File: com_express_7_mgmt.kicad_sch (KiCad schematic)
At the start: 79 parts, among them J11 Plug_Bus_CE7_EPT_401-51501-51, J14 PinHeader_1x3_P2.54mm_Drill1.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, J15 PinHeader_1x3_P2.54mm_Drill1.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, Q3 BSS138-7-F, Q4 BSS138-7-F, SW1 SW_1-1825027-1_THT, SW2 SW_1-1825027-1_THT, U24 M24C64-F_DFN8, U25 TPS3840PL30DBVR, U26 74AUP2G132, U27 MAX16150A_SOT, U28 74AUP2G132, U29 W25Q32FV_SOIC-8, U32 74AUP2G132

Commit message: Fix ERC
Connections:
- net ~{SUS_S3} is gone; now on an unnamed net: J11.A15 (~{SUS_S3})
- net ~{SUS_S5}: now also J11.A24 (~{SUS_S5})
- net at TP36.1: no longer J11.A24 (~{SUS_S5})
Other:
- moved on the sheet: R138, TP36
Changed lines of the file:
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@@
   (junction (at 259.08 205.74) (diameter 0) (color 0 0 0 0)
   )
+  (junction (at 91.44 68.58) (diameter 0) (color 0 0 0 0)
+  )
   (junction (at 254 121.92) (diameter 0) (color 0 0 0 0)
   )
@@
   (junction (at 342.9 62.23) (diameter 0) (color 0 0 0 0)
   )
+  (junction (at 382.27 193.04) (diameter 0) (color 0 0 0 0)
+  )
   (junction (at 78.74 53.34) (diameter 0) (color 0 0 0 0)
   )
@@
     (stroke (width 0) (type default))
   )
-  (wire (pts (xy 76.2 167.64) (xy 93.98 167.64))
+  (wire (pts (xy 104.14 38.1) (xy 104.14 41.91))
     (stroke (width 0) (type default))
   )
-  (wire (pts (xy 104.14 38.1) (xy 104.14 41.91))
+  (bus (pts (xy 105.41 266.7) (xy 95.25 266.7))
     (stroke (width 0) (type default))
   )
@@
     (stroke (width 0) (type default))
   )
-  (wire (pts (xy 334.645 231.14) (xy 349.885 231.14))
+  (wire (pts (xy 335.28 231.14) (xy 350.52 231.14))
     (stroke (width 0) (type default))
   )
@@
     (stroke (width 0) (type default))
   )
-  (bus (pts (xy 95.25 266.7) (xy 96.52 266.7))
-    (stroke (width 0) (type default))
-  )
   (wire (pts (xy 245.11 223.52) (xy 250.19 223.52))
     (stroke (width 0) (type default))
@@
     (stroke (width 0) (type default))
   )
+  (wire (pts (xy 95.25 172.72) (xy 76.2 172.72))
+    (stroke (width 0) (type default))
+  )
   (wire (pts (xy 119.38 147.32) (xy 121.92 147.32))
     (stroke (width 0) (type default))
@@
     (stroke (width 0) (type default))
   )
-  (wire (pts (xy 354.965 231.14) (xy 360.68 231.14))
+  (wire (pts (xy 355.6 231.14) (xy 360.68 231.14))
     (stroke (width 0) (type default))
   )
@@
     (effects (font (size 1.27 1.27)) (justify right bottom))
   )
+  (label "I2C{I2C}" (at 105.41 266.7 180) (fields_autoplaced)
+    (effects (font (size 1.27 1.27)) (justify right bottom))
+  )
   (label "~{RESBTN}" (at 332.74 57.15 0) (fields_autoplaced)
     (effects (font (size 1.27 1.27)) (justify left bottom))
   )
+  (label "~{SUS_S5}" (at 95.25 172.72 180) (fields_autoplaced)
+    (effects (font (size 1.27 1.27)) (justify right bottom))
+  )
   (label "~{TYPE1}" (at 201.93 137.16 0) (fields_autoplaced)
     (effects (font (size 1.27 1.27)) (justify left bottom))
@@
     (effects (font (size 1.27 1.27)) (justify right bottom))
   )
-  (label "~{SUS_S3}" (at 93.98 167.64 180) (fields_autoplaced)
-    (effects (font (size 1.27 1.27)) (justify right bottom))
-  )
   (label "~{TYPE2}" (at 83.82 218.44 180) (fields_autoplaced)
     (effects (font (size 1.27 1.27)) (justify right bottom))
@@
     (effects (font (size 1.27 1.27)) (justify left bottom))
   )
-  (label "~{BIOS_DIS0}" (at 334.645 231.14 0) (fields_autoplaced)
+  (label "~{BIOS_DIS0}" (at 335.28 231.14 0) (fields_autoplaced)
     (effects (font (size 1.27 1.27)) (justify left bottom))
   )
@@
     (effects (font (size 1.27 1.27)) (justify left))
   )
-  (hierarchical_label "I2C{I2C}" (shape output) (at 96.52 266.7 0) (fields_autoplaced)
-    (effects (font (size 1.27 1.27)) (justify left))
-  )
   (hierarchical_label "SMBus{I2C}" (shape output) (at 99.06 151.13 0) (fields_autoplaced)
     (effects (font (size 1.27 1.27)) (justify left))
@@
     )
   )
-  (symbol (lib_id "antmicroResistors0402:R_1k_0402") (at 349.885 231.14 0) (unit 1)
+  (symbol (lib_id "antmicroResistors0402:R_1k_0402") (at 350.52 231.14 0) (unit 1)
     (in_bom yes) (on_board yes) (dnp no)
-    (property "Reference" "R138" (at 347.345 229.87 0)
+    (property "Reference" "R138" (at 347.98 229.87 0)
       (effects (font (size 1.27 1.27) (thickness 0.15)))
     )
-    (property "Value" "R_1k_0402" (at 370.205 243.84 0)
+    (property "Value" "R_1k_0402" (at 370.84 243.84 0)
       (effects (font (size 1.27 1.27) (thickness 0.15)) (justify left bottom) hide)
     )
-    (property "Footprint" "antmicro-footprints:R_0402_1005Metric" (at 370.205 246.38 0)
+    (property "Footprint" "antmicro-footprints:R_0402_1005Metric" (at 370.84 246.38 0)
       (effects (font (size 1.27 1.27) (thickness 0.15)) (justify left bottom) hide)
     )
-    (property "Datasheet" "https://www.bourns.com/docs/product-datasheets/cr.pdf" (at 370.205 248.92 0)
+    (property "Datasheet" "https://www.bourns.com/docs/product-datasheets/cr.pdf" (at 370.84 248.92 0)
       (effects (font (size 1.27 1.27) (thickness 0.15)) (justify left bottom) hide)
     )
-    (property "MPN" "CR0402-FX-1001GLF" (at 370.205 251.46 0)
+    (property "MPN" "CR0402-FX-1001GLF" (at 370.84 251.46 0)
       (effects (font (size 1.27 1.27) (thickness 0.15)) (justify left bottom) hide)
     )
-    (property "Manufacturer" "Bourns" (at 370.205 254 0)
+    (property "Manufacturer" "Bourns" (at 370.84 254 0)
       (effects (font (size 1.27 1.27) (thickness 0.15)) (justify left bottom) hide)
     )
-    (property "License" "Apache-2.0" (at 370.205 256.54 0)
+    (property "License" "Apache-2.0" (at 370.84 256.54 0)
       (effects (font (size 1.27 1.27) (thickness 0.15)) (justify left bottom) hide)
     )
-    (property "Author" "Antmicro" (at 370.205 259.08 0)
+    (property "Author" "Antmicro" (at 370.84 259.08 0)
       (effects (font (size 1.27 1.27) (thickness 0.15)) (justify left bottom) hide)
     )
-    (property "Val" "1k" (at 356.235 229.87 0)
+    (property "Val" "1k" (at 356.87 229.87 0)
       (effects (font (size 1.27 1.27) (thickness 0.15)))
     )
-    (property "Tolerance" "1%" (at 370.205 241.3 0)
+    (property "Tolerance" "1%" (at 370.84 241.3 0)
       (effects (font (size 1.27 1.27)) (justify left bottom) hide)
     )
@@
     )
   )
+  (symbol (lib_id "antmicropower:PWR_FLAG") (at 382.27 193.04 0) (unit 1)
+    (in_bom yes) (on_board yes) (dnp no) (fields_autoplaced)
+    (property "Reference" "#FLG016" (at 382.27 191.135 0)
+      (effects (font (size 1.27 1.27)) hide)
+    )
+    (property "Value" "PWR_FLAG" (at 382.27 187.96 0)
+      (effects (font (size 1.27 1.27)) hide)
+    )
+    (property "Footprint" "" (at 382.27 193.04 0)
+      (effects (font (size 1.27 1.27)) hide)
+    )
+    (property "Datasheet" "" (at 382.27 193.04 0)
+      (effects (font (size 1.27 1.27)) hide)
+    )
+    (pin "1")
+    (instances
+      (project "com-express-7-baseboard"
+        (path "/1b8c34da-dad5-4b0b-8c4b-45db766c4dfa/ec04a123-aeba-4efb-8d03-9c06245c1fcc"
+          (reference "#FLG016") (unit 1)
+        )
+      )
+    )
+  )
   (symbol (lib_id "antmicroTestPoints:TP_0.75mm_SMD") (at 76.2 124.46 0) (unit 1)
     (in_bom no) (on_board yes) (dnp no) (fields_autoplaced)
@@
     )
   )
+  (symbol (lib_id "antmicropower:PWR_FLAG") (at 91.44 68.58 270) (unit 1)
+    (in_bom yes) (on_board yes) (dnp no) (fields_autoplaced)
+    (property "Reference" "#FLG017" (at 93.345 68.58 0)
+      (effects (font (size 1.27 1.27)) hide)
+    )
+    (property "Value" "PWR_FLAG" (at 95.25 68.5799 90)
+      (effects (font (size 1.27 1.27)) (justify left) hide)
+    )
+    (property "Footprint" "" (at 91.44 68.58 0)
+      (effects (font (size 1.27 1.27)) hide)
+    )
+    (property "Datasheet" "" (at 91.44 68.58 0)
+      (effects (font (size 1.27 1.27)) hide)
+    )
+    (pin "1")
+    (instances
+      (project "com-express-7-baseboard"
+        (path "/1b8c34da-dad5-4b0b-8c4b-45db766c4dfa/ec04a123-aeba-4efb-8d03-9c06245c1fcc"
+          (reference "#FLG017") (unit 1)
+        )
+      )
+    )
+  )
   (symbol (lib_name "BAT54C_1") (lib_id "antmicroDiodesRectifiersSingle:BAT54C") (at 135.89 63.5 180) (unit 1)
     (in_bom yes) (on_board yes) (dnp no) (fields_autoplaced)
@@
     )
   )
-  (symbol (lib_id "antmicroTestPoints:TP_0.75mm_SMD") (at 76.2 172.72 0) (unit 1)
+  (symbol (lib_id "antmicroTestPoints:TP_0.75mm_SMD") (at 76.2 167.64 0) (unit 1)
     (in_bom no) (on_board yes) (dnp no) (fields_autoplaced)
-    (property "Reference" "TP36" (at 81.28 172.72 0)
+    (property "Reference" "TP36" (at 81.28 167.64 0)
       (effects (font (size 1.27 1.27) (thickness 0.15)) (justify left))
     )
-    (property "Value" "TP_0.75mm_SMD" (at 86.995 176.53 0)
+    (property "Value" "TP_0.75mm_SMD" (at 86.995 171.45 0)
       (effects (font (size 1.27 1.27) (thickness 0.15)) (justify left bottom) hide)
     )
-    (property "Footprint" "antmicro-footprints:TP_SMD_0.75mm" (at 86.995 179.07 0)
+    (property "Footprint" "antmicro-footprints:TP_SMD_0.75mm" (at 86.995 173.99 0)
       (effects (font (size 1.27 1.27) (thickness 0.15)) (justify left bottom) hide)
     )
-    (property "Datasheet" "" (at 93.98 185.42 0)
+    (property "Datasheet" "" (at 93.98 180.34 0)
       (effects (font (size 1.27 1.27) (thickness 0.15)) (justify left bottom) hide)
     )
-    (property "MPN" "" (at 86.995 184.15 0)
+    (property "MPN" "" (at 86.995 179.07 0)
       (effects (font (size 1.27 1.27) (thickness 0.15)) (justify left bottom) hide)
     )
-    (property "Manufacturer" "" (at 86.995 179.07 0)
+    (property "Manufacturer" "" (at 86.995 173.99 0)
       (effects (font (size 1.27 1.27) (thickness 0.15)) (justify left bottom) hide)
     )
-    (property "Author" "Antmicro" (at 86.995 181.61 0)
+    (property "Author" "Antmicro" (at 86.995 176.53 0)
       (effects (font (size 1.27 1.27) (thickness 0.15)) (justify left bottom) hide)
     )
-    (property "License" "Apache-2.0" (at 86.995 184.15 0)
+    (property "License" "Apache-2.0" (at 86.995 179.07 0)
       (effects (font (size 1.27 1.27) (thickness 0.15)) (justify left bottom) hide)
     )

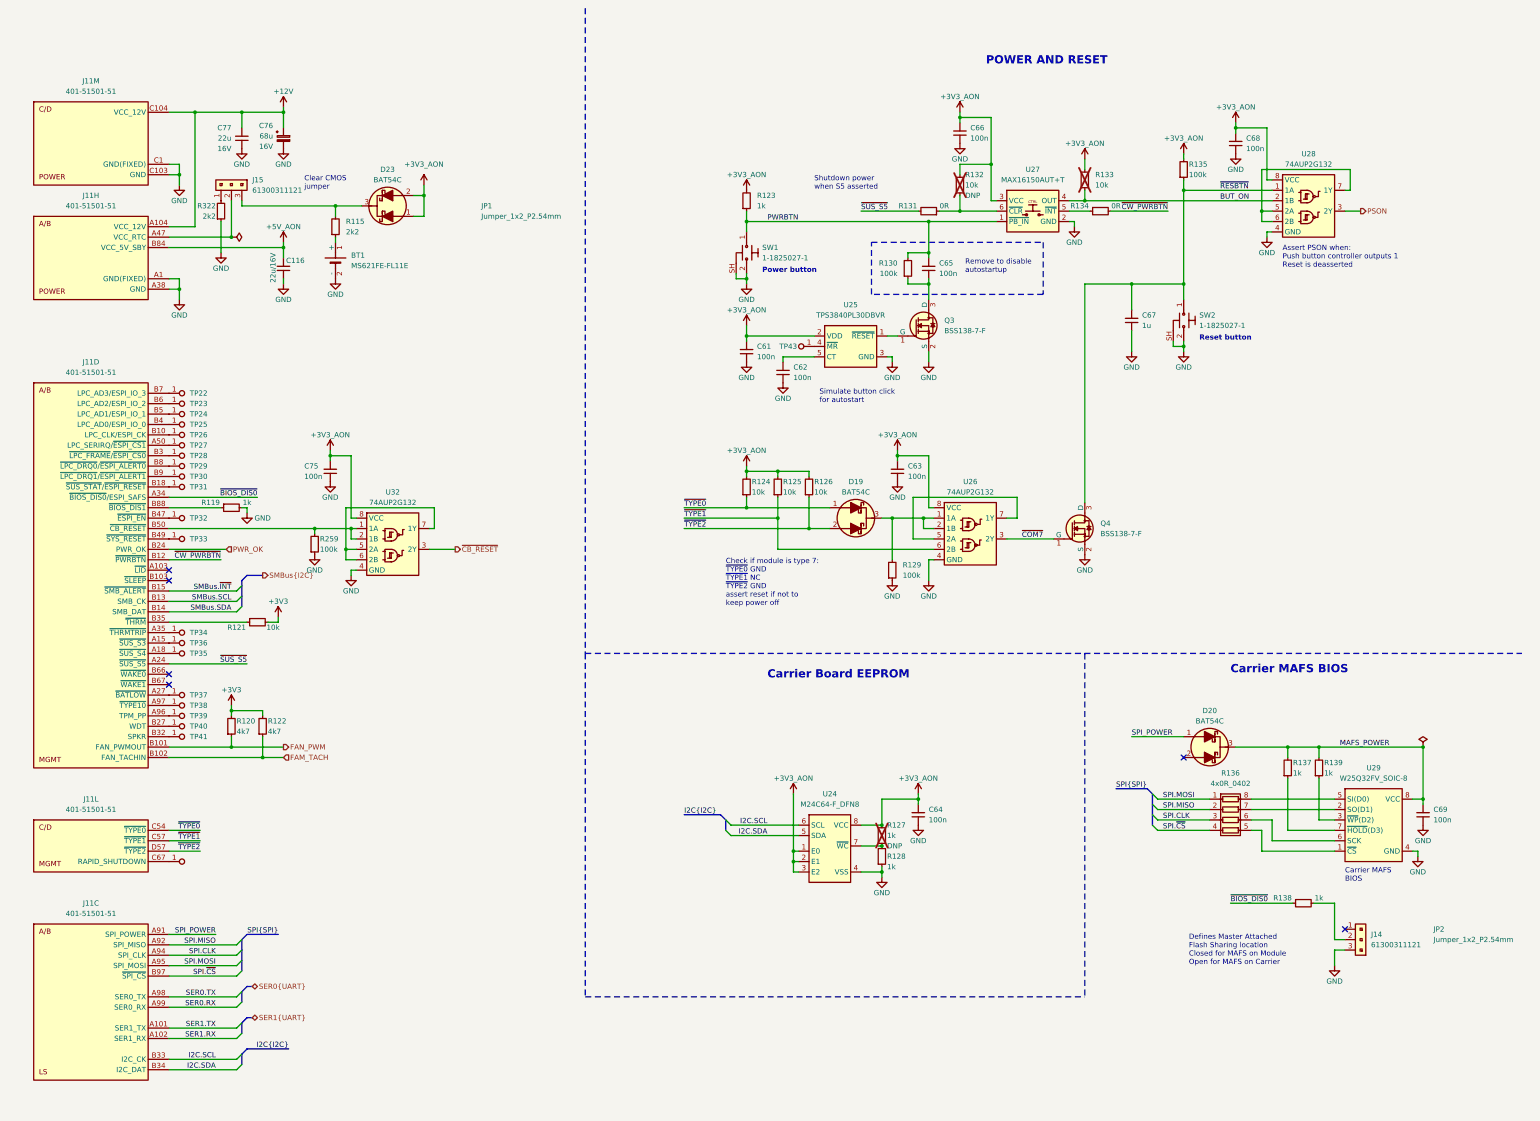
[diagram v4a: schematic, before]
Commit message: Reannotate schematic
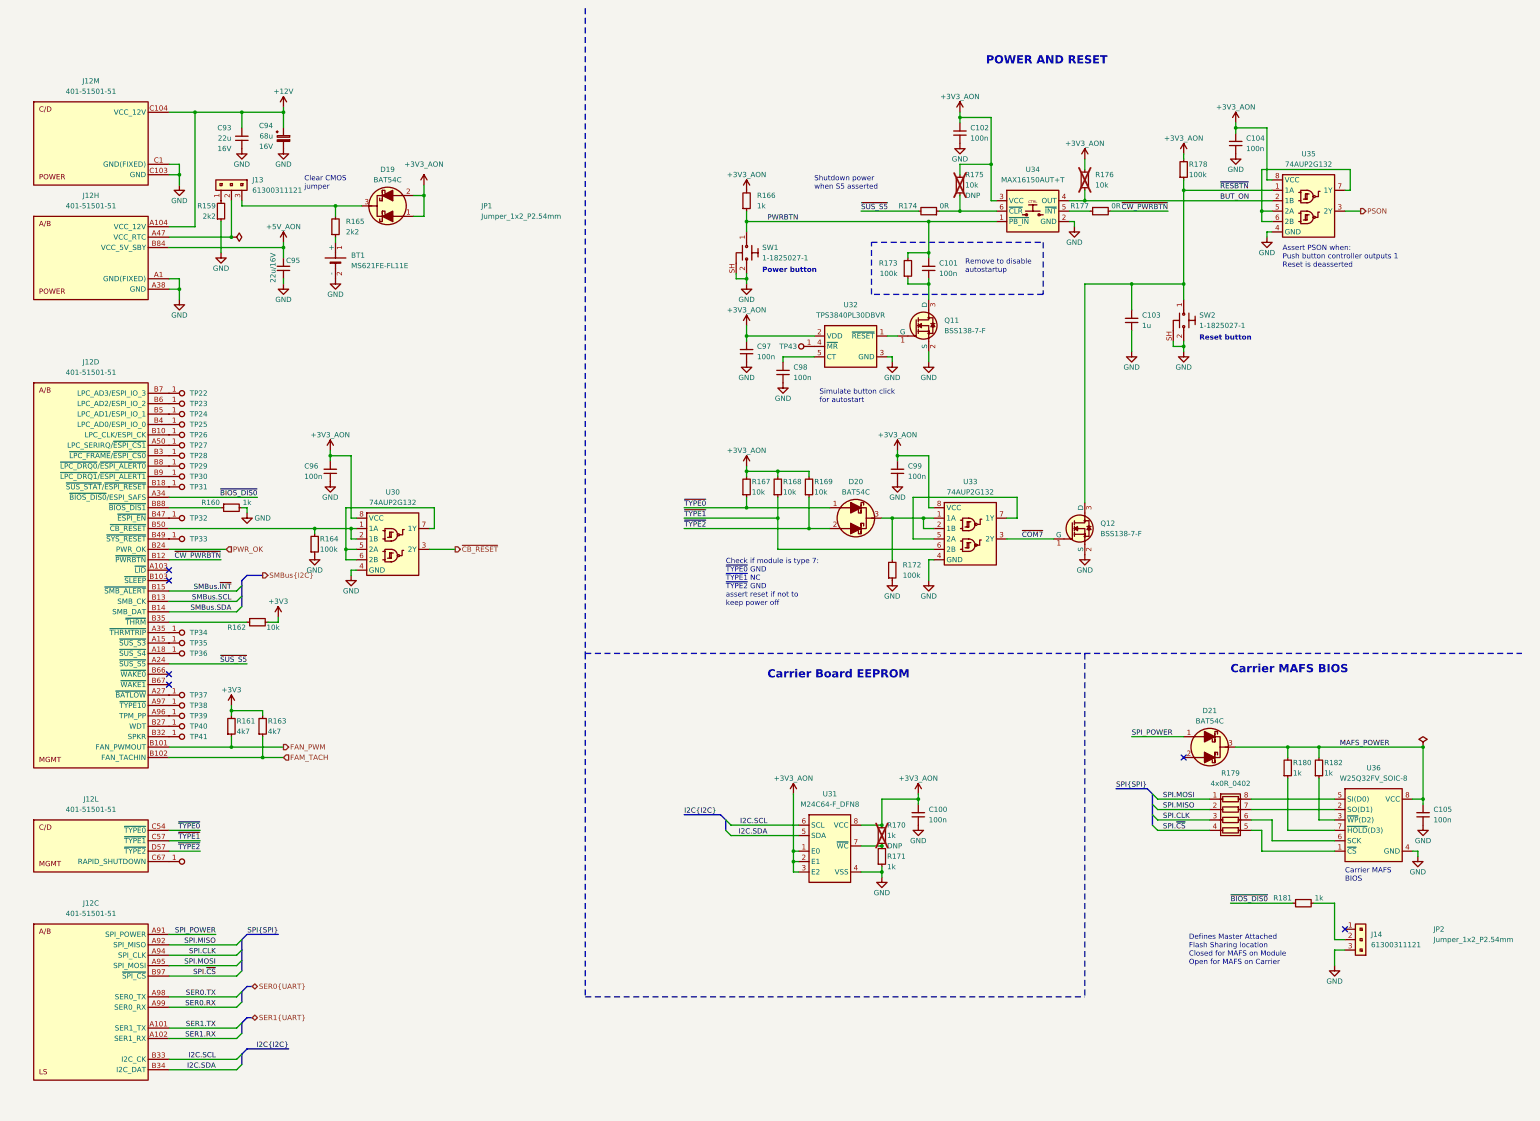
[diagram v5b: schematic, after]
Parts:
- renumbered C64 to C100, C65 to C101, C66 to C102, C67 to C103, C68 to C104, C69 to C105, C77 to C93, C76 to C94, C116 to C95, C75 to C96, C61 to C97, C62 to C98, C63 to C99, D23 to D19, D19 to D20, D20 to D21, J11 to J12, J15 to J13, Q3 to Q11, Q4 to Q12, R322 to R159, R119 to R160, R120 to R161, R121 to R162, R122 to R163, R259 to R164, R115 to R165, R123 to R166, R124 to R167, R125 to R168, R126 to R169, R127 to R170, R128 to R171, R129 to R172, R130 to R173, R131 to R174, R132 to R175, R133 to R176, R134 to R177, R135 to R178, R136 to R179, R137 to R180, R138 to R181, R139 to R182, TP36 to TP35, TP35 to TP36, U32 to U30, U24 to U31, U25 to U32, U26 to U33, U27 to U34, U28 to U35, U29 to U36

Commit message: Optimize BOM, reannotate
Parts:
- removed R161, R163: R_4k7_0402, antmicro-footprints:R_0402_1005Metric, symbol antmicroResistors0402:R_4k7_0402
- removed R179: 4x0R_0402_array, antmicro-footprints:4x0R_0402_array_EXB28V, symbol antmicroResistorNetworksArrays:4x0R_0402_array
- added R161, R163: R_5k1_0402, antmicro-footprints:R_0402_1005Metric, symbol antmicroResistors0402:R_5k1_0402
- renumbered R180 to R179, R181 to R180, R182 to R181
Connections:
- net +3V3: now also R161.2, R163.2
- net FAM_TACH: now also R163.1
- net FAN_PWM: now also R161.1
- net SPI.CLK: now also U36.6 (SCK)
- net SPI.MISO: now also U36.2 (SO(D1))
- net SPI.MOSI: now also U36.5 (SI(D0))
- net SPI.~{CS}: now also U36.1 (~{CS})

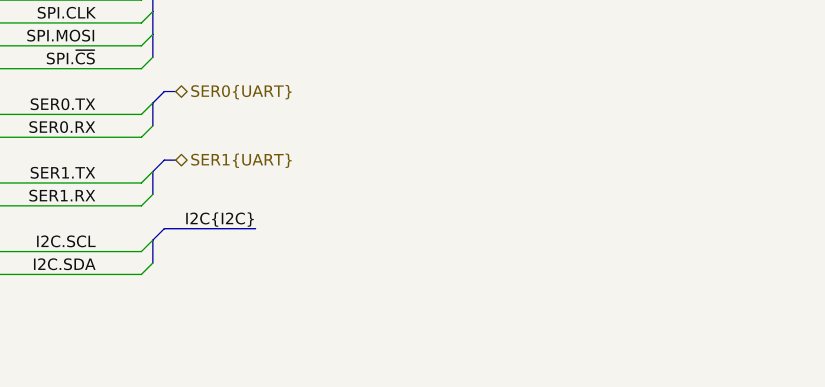
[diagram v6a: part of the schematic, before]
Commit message: [#58137] Add power monitors; clean up I2C bus
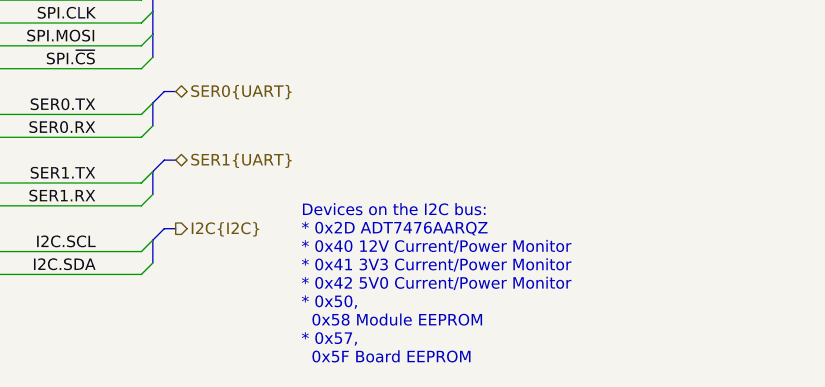
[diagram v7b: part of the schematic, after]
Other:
- note added: "Devices on the I2C bus: * 0x2D ADT7476AARQZ * 0x40 12V Current/Power Monitor * 0x41 3V3 Current/Power Monitor * 0x42 5V0 Current/Power Monitor * 0x50, 0x58 Module EEPROM * 0x57, 0x5F Board EEPROM"
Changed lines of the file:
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@@
     (stroke (width 0) (type default))
   )
-  (bus (pts (xy 105.41 266.7) (xy 95.25 266.7))
+  (bus (pts (xy 96.52 266.7) (xy 95.25 266.7))
     (stroke (width 0) (type default))
   )
@@
     (effects (font (size 1.27 1.27)) (justify left bottom))
   )
+  (text "Devices on the I2C bus:\n* 0x2D ADT7476AARQZ\n* 0x40 12V Current/Power Monitor\n* 0x41 3V3 Current/Power Monitor\n* 0x42 5V0 Current/Power Monitor \n* 0x50, \n  0x58 Module EEPROM \n* 0x57,\n  0x5F Board EEPROM\n"
+    (at 110.49 281.94 0)
+    (effects (font (size 1.27 1.27)) (justify left bottom))
+  )
   (label "SER1.RX" (at 87.63 264.16 180) (fields_autoplaced)
-    (effects (font (size 1.27 1.27)) (justify right bottom))
-  )
-  (label "I2C{I2C}" (at 105.41 266.7 180) (fields_autoplaced)
     (effects (font (size 1.27 1.27)) (justify right bottom))
   )
@@
     (effects (font (size 1.27 1.27)) (justify left))
   )
+  (hierarchical_label "I2C{I2C}" (shape output) (at 96.52 266.7 0) (fields_autoplaced)
+    (effects (font (size 1.27 1.27)) (justify left))
+  )
